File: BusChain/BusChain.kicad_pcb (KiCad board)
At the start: 2 copper layers, 50 x 35 mm, 33 parts, among them J1 Bonn_01x07, J10 Bonn_01x04, J11 Bonn_01x04, J12 Bonn_01x04, J13 Bonn_01x04, J14 Bonn_01x04, J15 Bonn_01x04, J16 Bonn_01x04, J17 Bonn_01x04, J18 Bonn_01x07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

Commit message: Finalized PCBs for fabrication
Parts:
- removed G***: LOGO, Touchstone:logo
- added C1: 0.1u, Capacitor_SMD:C_0402_1005Metric, F.Cu at (24.9, 22.0)
- added C2: 0.1u, Capacitor_SMD:C_0402_1005Metric, F.Cu at (29.4, 22.0)
- added REF**: Mounting_Hole, Touchstone:Mounting_Hole, F.Cu at (27.1, 28.6)
- added REF**: Mounting_Hole, Touchstone:Mounting_Hole, F.Cu at (58.1, 50.0)
- added U2: MIC5365-3.3YC5, Package_TO_SOT_SMD:SOT-353_SC-70-5, F.Cu at (27.1, 22.5)
- R1, R2: value 1.2K -> 500
- moved R1 32.1 mm to (19.5, 41.5), turned to 90 degrees
- moved J18 4.75 mm to (70.5, 22.0)
- moved J1 4.70 mm to (19.5, 22.0)
- moved D1 4.35 mm to (69.0, 47.5)
- moved D2 4.35 mm to (69.0, 50.1)
- moved D3 4.35 mm to (69.0, 52.7)
- moved R3 4.35 mm to (71.9, 47.5)
- moved R4 4.35 mm to (71.9, 50.1)
- moved R5 4.35 mm to (71.9, 52.7)
- moved R2 2.11 mm to (29.5, 33.3), turned to 90 degrees
- renumbered C1 to C3, C2 to C4, C3 to C5, U1 to U4, U2 to U5, U3 to U6
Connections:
- J1 pad 1: /VCC -> /V?
- R1 pad 1: /SDA -> /VCC
- R1 pad 2: /VCC -> /SDA
- R2 pad 1: /SCL -> /VCC
- R2 pad 2: /VCC -> /SCL
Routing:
- net /VCC: track 186.4 -> 227.2 mm, vias 0 -> 1
- net /SDA: track 65.0 -> 84.4 mm
- net /RCLK: track 79.1 -> 93.5 mm
- net /CLK: track 75.3 -> 89.5 mm
- net /V?: track 0.00 -> 6.99 mm
- net /SCL: track 65.8 -> 59.7 mm
- net /SIN: track 39.7 -> 44.4 mm
- net /ENA: track 26.9 -> 31.3 mm
- net GND: track 10.7 -> 13.8 mm, vias 10 -> 12
- net /ENB: track 47.4 -> 49.9 mm
- net /SOUT: track 11.5 -> 13.5 mm
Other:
- board size 50 x 35 mm -> 60 x 35 mm
- board text added: "A0"
- board text added: "A1"
- board text added: "A2"
- board text added: "A3"
- board text added: "A4"
- board text added: "A5"
- board text added: "A6"
- board text added: "A7"
- board text added: "B0"
- board text added: "B1"
- board text added: "B2"
- board text added: "B3"
- board text added: "B4"
- board text added: "B5"
- board text added: "B6"
- board text added: "B7"
- board text added: "ENA"
- board text added: "ENB"
- board text added: "V?"
- board text removed: "0"
- board text removed: "0-7"
- board text removed: "1"
- board text removed: "10"
- board text removed: "11"
- board text removed: "12"
- board text removed: "13"
- board text removed: "14"
- board text removed: "15"
- board text removed: "2"
- board text removed: "3"
- board text removed: "4"
- board text removed: "5"
- board text removed: "6"
- board text removed: "7"
- board text removed: "8"
- board text removed: "8-15"
- board text removed: "9"

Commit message: Resolved various production and testing issues
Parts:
- removed REF** (x2): Mounting_Hole, Touchstone:Mounting_Hole
- J1, J18: value Bonn_01x07 -> Conn_01x07
- J10, J11, J12, J13, J14, J15, J16, J17, J2, J3, J4, J5, J6, J7, J8, J9: value Bonn_01x04 -> Conn_01x04
- R1, R2: value 500 -> 1.2K
- U4: value 74HB595 -> 74HC595
- U5, U6: value TBB9548BPWR -> TCA9548BPWR
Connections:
- U2 pad 3: unconnected-(U2-EN-Pad3) -> /V?
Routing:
- net /V?: track 6.99 -> 9.47 mm

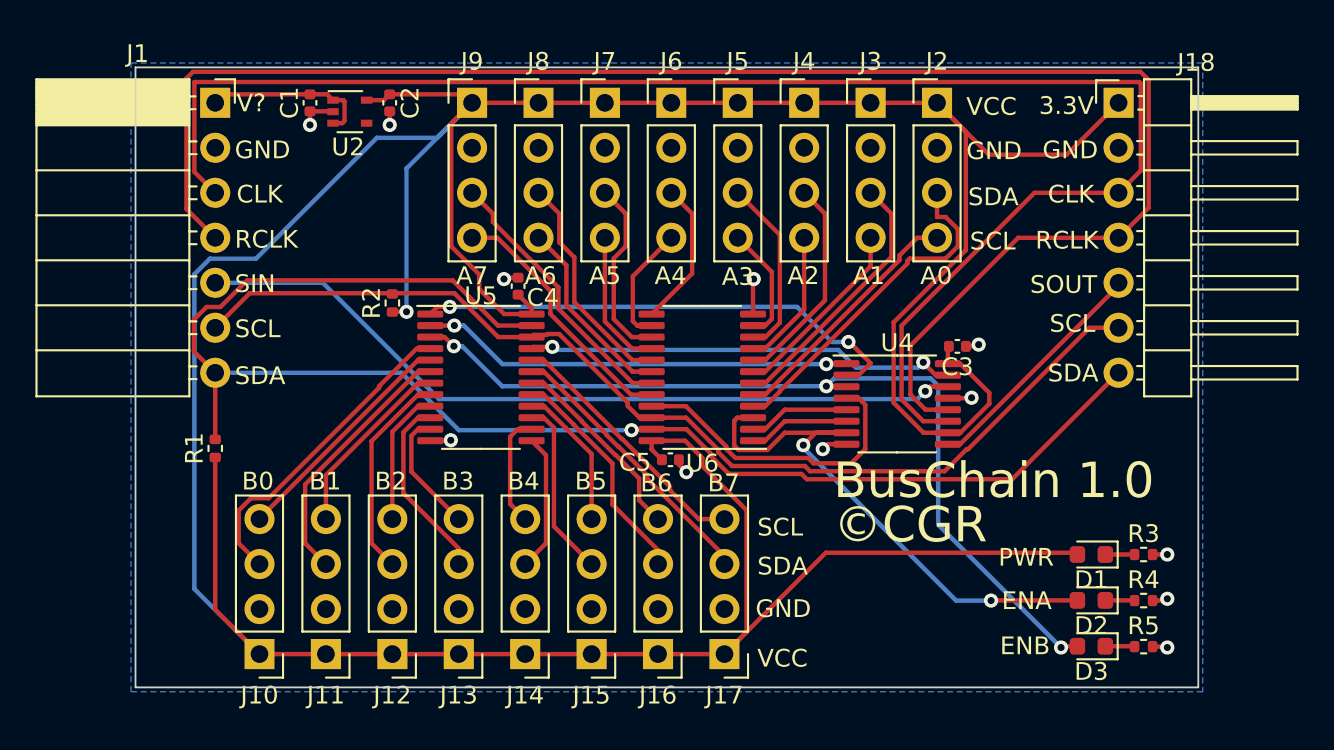
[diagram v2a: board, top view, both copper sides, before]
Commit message: Finished BusChain1.1 and added power daisy-chaining option
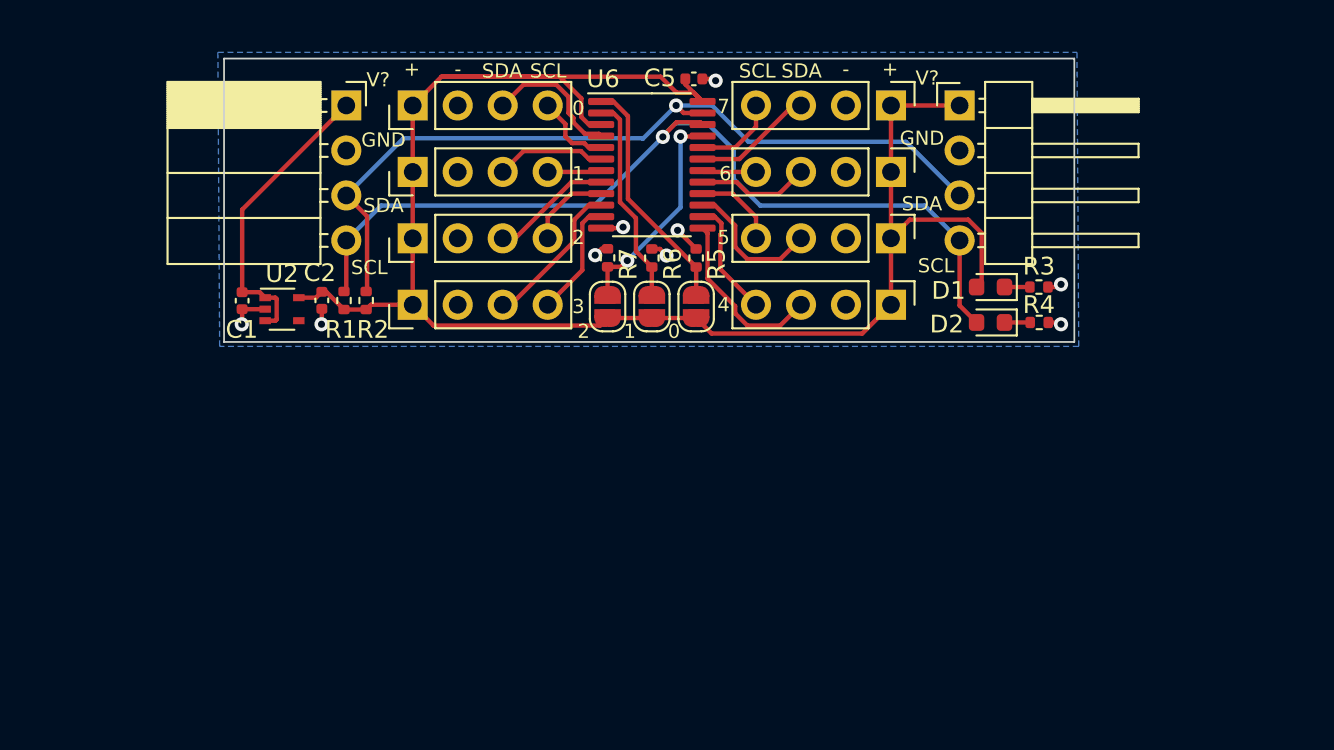
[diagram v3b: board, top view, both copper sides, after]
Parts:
- removed C3, C4: 0.1u, Capacitor_SMD:C_0402_1005Metric
- removed D3: LED, LED_SMD:LED_0603_1608Metric
- removed J11, J12, J13, J14, J15, J16, J17: Conn_01x04, Connector_PinHeader_2.54mm:PinHeader_1x04_P2.54mm_Vertical
- removed J18: Conn_01x07, Connector_PinHeader_2.54mm:PinHeader_1x07_P2.54mm_Horizontal
- removed U4: 74HC595, Package_SO:TSSOP-16_4.4x5mm_P0.65mm
- removed U5: TCA9548BPWR, Package_SO:TSSOP-24_4.4x7.8mm_P0.65mm
- added JP1: Jumper_2_Open, Jumper:SolderJumper-2_P1.3mm_Open_RoundedPad1.0x1.5mm, F.Cu at (41.6, 33.5)
- added JP2: Jumper_2_Open, Jumper:SolderJumper-2_P1.3mm_Open_RoundedPad1.0x1.5mm, F.Cu at (44.1, 33.5)
- added JP3: Jumper_2_Open, Jumper:SolderJumper-2_P1.3mm_Open_RoundedPad1.0x1.5mm, F.Cu at (46.6, 33.5)
- added R6: 10K, Resistor_SMD:R_0402_1005Metric, F.Cu at (44.1, 30.8)
- added R7: 10K, Resistor_SMD:R_0402_1005Metric, F.Cu at (41.6, 30.8)
- J1: value Conn_01x07 -> Conn_01x04; footprint Connector_PinSocket_2.54mm:PinSocket_1x07_P2.54mm_Horizontal -> Connector_PinSocket_2.54mm:PinSocket_1x04_P2.54mm_Horizontal
- J10: footprint Connector_PinHeader_2.54mm:PinHeader_1x04_P2.54mm_Vertical -> Connector_PinHeader_2.54mm:PinHeader_1x04_P2.54mm_Horizontal
- R5: value 500 -> 10K
- moved J10 50.2 mm to (61.5, 22.1), turned to 0 degrees
- moved R5 33.5 mm to (46.6, 30.8), turned to -90 degrees
- moved J2 29.6 mm to (30.6, 22.1), turned to 90 degrees
- moved J3 26.1 mm to (30.6, 25.9), turned to 90 degrees
- moved J9 23.7 mm to (57.6, 22.1), turned to -90 degrees
- moved J4 23.4 mm to (30.6, 29.6), turned to 90 degrees
- moved J5 21.6 mm to (30.6, 33.4), turned to 90 degrees
- moved C5 21.5 mm to (46.5, 20.6)
- moved J8 20.3 mm to (57.6, 25.9), turned to -90 degrees
- moved J7 17.9 mm to (57.6, 29.6), turned to -90 degrees
- moved J6 16.8 mm to (57.6, 33.4), turned to -90 degrees
- moved R4 16.8 mm to (66.0, 34.4)
- moved D2 16.7 mm to (63.3, 34.4)
- moved R3 16.2 mm to (66.0, 32.4)
- moved D1 16.1 mm to (63.3, 32.4)
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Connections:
- net /SC0A renamed /SC0
- net /SC1A renamed /SC1
- net /SC2A renamed /SC2
- net /SC3A renamed /SC3
- net /SC4A renamed /SC4
- net /SC5A renamed /SC5
- net /SC6A renamed /SC6
- net /SC7A renamed /SC7
- net /SD0A renamed /SD0
- net /SD1A renamed /SD1
- net /SD2A renamed /SD2
- net /SD3A renamed /SD3
- net /SD4A renamed /SD4
- net /SD5A renamed /SD5
- net /SD6A renamed /SD6
- net /SD7A renamed /SD7
- D2 pad 2: /ENA -> /SCL
- J1 pad 3: /CLK -> /SDA
- J1 pad 4: /RCLK -> /SCL
- J10 pad 3: /SD0B -> /SDA
- J10 pad 4: /SC0B -> /SCL
- R1 pad 2: /SDA -> /SCL
- R2 pad 2: /SCL -> /SDA
- R5 pad 1: Net-(D3-K) -> GND
- R5 pad 2: GND -> Net-(JP3-B)
- U6 pad 1: Net-(U4-QG) -> Net-(JP3-B)
- U6 pad 3: /ENA -> /VCC
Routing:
- net /VCC: track 227.2 -> 101.2 mm, vias 1 -> 0
- net /RCLK: track 93.5 -> 0.00 mm
- net /CLK: track 89.5 -> 0.00 mm
- net /ENB: track 49.9 -> 0.00 mm, vias 3 -> 0
- net /SIN: track 44.4 -> 0.00 mm, vias 1 -> 0
- net /SDA: track 84.4 -> 46.5 mm
- net /ENA: track 31.3 -> 0.00 mm, vias 2 -> 0
- net Net-(U4-QC): track 28.0 -> 0.00 mm, vias 2 -> 0
- net Net-(U4-QA): track 24.5 -> 0.00 mm, vias 2 -> 0
- net Net-(U4-QB): track 24.4 -> 0.00 mm, vias 2 -> 0
- net /SD0B: track 18.2 -> 0.00 mm
- net /SD7B: track 15.8 -> 0.00 mm
- net /SC7B: track 14.8 -> 0.00 mm
- net /SD1B: track 14.7 -> 0.00 mm
- net Net-(JP3-B): track 0.00 -> 13.5 mm
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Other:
- board size 60 x 35 mm -> 48 x 16 mm
- board text added: "+"
- board text added: "-"
- board text added: "0"
- board text added: "1"
- board text added: "2"
- board text added: "3"
- board text added: "4"
- board text added: "5"
- board text added: "6"
- board text added: "7"
- board text added: "BusChain 1.1"
- board text removed: "3.3V"
- board text removed: "A0"
- board text removed: "A1"
- board text removed: "A2"
- board text removed: "A3"
- board text removed: "A4"
- board text removed: "A5"
- board text removed: "A6"
- board text removed: "A7"
- board text removed: "B0"
- board text removed: "B1"
- board text removed: "B2"
- board text removed: "B3"
- board text removed: "B4"
- board text removed: "B5"
- board text removed: "B6"
- board text removed: "B7"
- board text removed: "BusChain 1.0"
- board text removed: "CLK"
- board text removed: "ENA"
- board text removed: "ENB"
- board text removed: "PWR"
- board text removed: "RCLK"
- board text removed: "SIN"
- board text removed: "SOUT"
- board text removed: "VCC"
